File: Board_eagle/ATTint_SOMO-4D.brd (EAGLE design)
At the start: 32.1 x 31.1 mm, 18 parts, among them U1 SOMO-14D, U2 MAX1555, X2 STEREOJACK, X3 USB-SMD-NS

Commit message: Code cleaning
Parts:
- added R1: 1K, spark-fun:0805
- moved C1 17.9 mm to (29.8, 11.1), turned to 90 degrees
- moved LED1 6.75 mm to (1.91, 24.8), turned to 0 degrees
- moved R6 6.38 mm to (4.45, 29.2)
- moved R7 5.43 mm to (29.2, 14.9), flipped to the top
- moved C4 5.26 mm to (26.0, 2.22), turned to 0 degrees
- moved U$3 4.32 mm to (26.0, 8.26), turned to 180 degrees
- moved U2 3.88 mm to (8.26, 24.8)
- moved SENSOR 3.55 mm to (26.4, 19.1), turned to 0 degrees
- moved C9 2.93 mm to (4.76, 19.7)
- moved X3 2.03 mm to (4.76, 24.8), turned to 0 degrees
- moved AUDIO1 1.27 mm to (6.99, 12.4)
- moved JP3 1.27 mm to (26.4, 6.03)
- moved SWITCH1 0.95 mm to (27.9, 25.4)
- moved C7 0.90 mm to (10.2, 21.0), turned to 270 degrees
- moved U1 0.63 mm to (10.8, 8.89)
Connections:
- net CLOCK: now also U$6.6; no longer U$6.5
- net DATA: now also U$6.7; no longer U$6.6
- net RESET: now also U$6.5; no longer U$6.7
- net SWITCH: now also R1.2
- net VCC: now also R1.1
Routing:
- net VCHARGE: track 85.1 -> 52.4 mm
- net AUDIO_B: track 0.00 -> 21.4 mm
- net VCC: track 28.5 -> 47.0 mm
- net RESET: track 0.00 -> 17.5 mm
- net DATA: track 0.00 -> 15.1 mm
- net AUDIO_A: track 9.68 -> 19.3 mm
- net SWITCH: track 11.7 -> 20.2 mm
- net N$6: track 10.4 -> 15.3 mm
- net N$7: track 10.8 -> 6.26 mm
- net N$8: track 2.49 -> 4.66 mm
- net SENSOR: track 20.5 -> 19.5 mm
- net NRESET: track 5.61 -> 4.65 mm
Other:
- board size 32.1 x 31.1 mm -> 31.1 x 31.1 mm
- board text added: "Audio"
- board text added: "Textile"
- board text removed: "Audio textile"

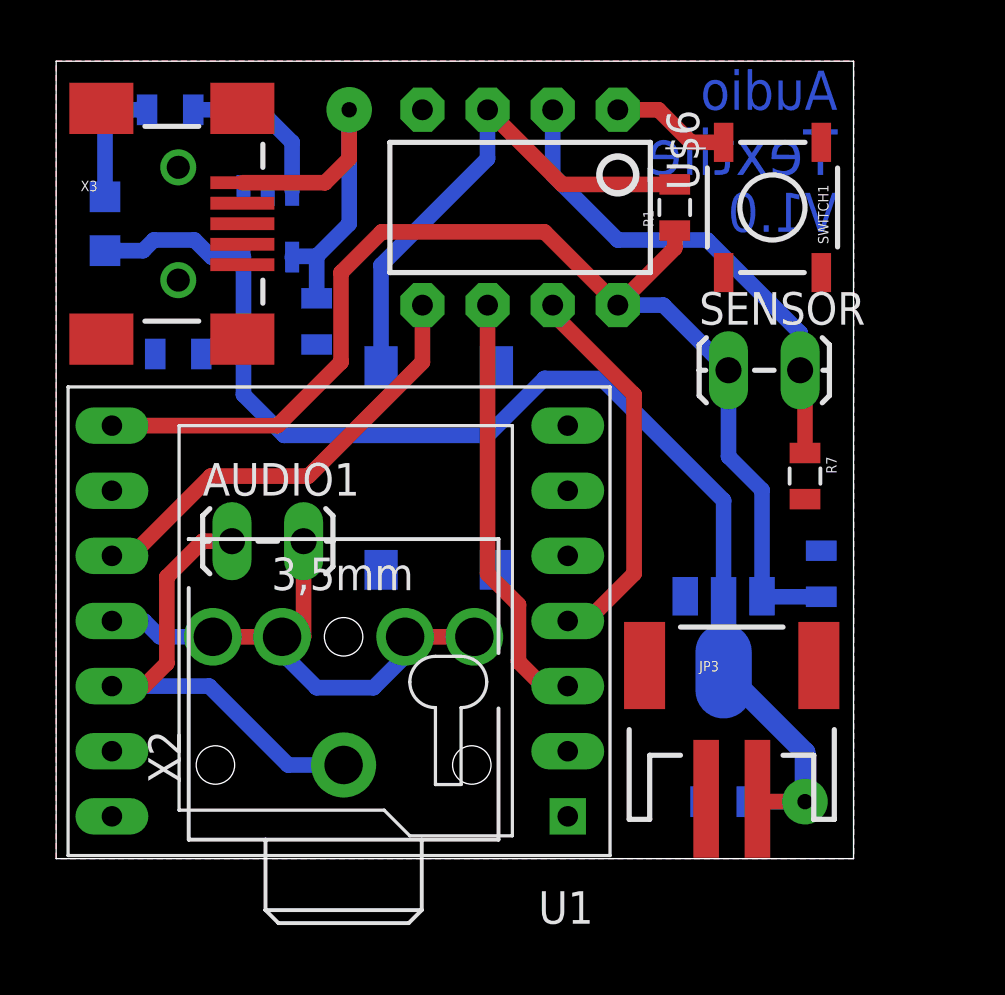
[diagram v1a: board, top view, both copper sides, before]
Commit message: optimised sleeping consumption
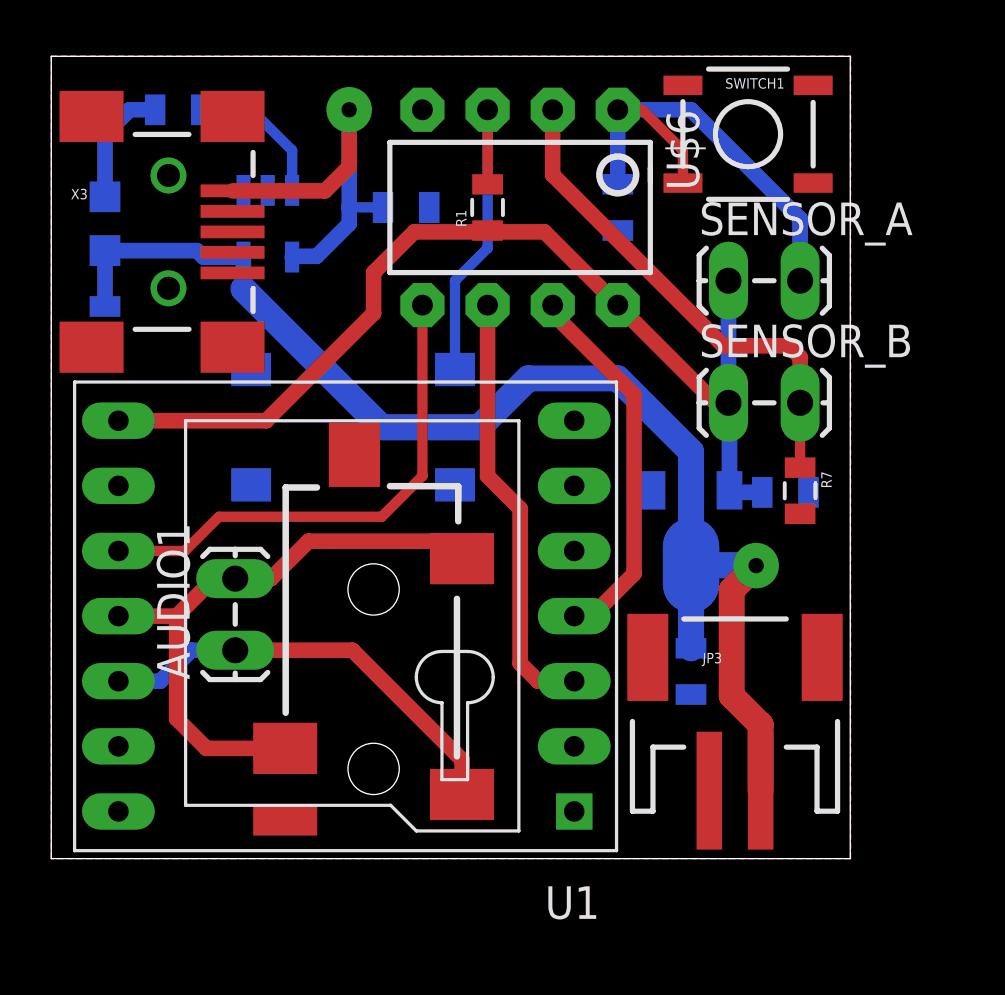
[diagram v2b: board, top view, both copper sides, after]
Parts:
- removed SENSOR: 3.3V, charles:1X02_LOCK_LONGPADS
- removed X2: STEREOJACK, adafruit:STX3100
- added R2: 1K, spark-fun:0805
- added SENSOR_A, SENSOR_B: 3.3V, charles:1X02_LOCK_LONGPADS
- added U3: (no value), SparkFun:AUDIO-JACK-3.5MM-SMD
- moved R1 7.30 mm to (16.8, 25.4)
- moved C7 5.65 mm to (13.7, 25.4), turned to 180 degrees
- moved C4 5.24 mm to (24.8, 7.30), turned to 270 degrees
- moved U$3 4.32 mm to (24.8, 12.4)
- moved AUDIO1 4.13 mm to (6.99, 8.26), turned to 90 degrees
- moved SWITCH 3.70 mm to (11.6, 16.8), turned to 180 degrees
- moved C1 3.47 mm to (28.4, 14.3), turned to 180 degrees
- moved SWITCH1 3.01 mm to (27.0, 28.3), turned to 0 degrees
- moved C9 3.01 mm to (1.91, 20.6), turned to 270 degrees
- moved R7 0.60 mm to (29.0, 14.4)
- moved X3 0.50 mm to (4.38, 24.4)
- moved JP3 0.34 mm to (26.5, 6.35)
- moved R6 0.32 mm to (4.76, 29.2)
- moved U1 0.32 mm to (11.0, 9.08)
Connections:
- net AUDIO_A: now also U3.SLEEVE; no longer X2.1
- net AUDIO_B: now also U3.RING, U3.TIP; no longer X2.2, X2.3, X2.4, X2.5
- net GND: now also R2.2
- net NRESET: now also R2.1, SENSOR_A.2
- net SENSOR: now also SENSOR_B.2; no longer SENSOR.2
- net VCC: now also SENSOR_A.1, SENSOR_B.1; no longer SENSOR.1
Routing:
- net NRESET: track 4.65 -> 18.7 mm
- net SWITCH: track 20.2 -> 13.6 mm
- net VCC: track 47.0 -> 40.7 mm
- net AUDIO_A: track 19.3 -> 17.0 mm
- net RESET: track 17.5 -> 19.7 mm
- net AUDIO_B: track 21.4 -> 23.6 mm
- net VCHARGE: track 52.4 -> 50.4 mm
- net N$7: track 6.26 -> 5.76 mm
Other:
- board size 31.1 x 31.1 mm -> 31.2 x 31.3 mm
- board text added: "01/06/2012"
- board text added: "26846856"
- board text added: "Fabric"
- board text added: "Sonic"
- board text removed: "Audio"
- board text removed: "Textile"
